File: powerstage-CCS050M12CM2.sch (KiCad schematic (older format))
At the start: 34 parts, among them J13 CONN_01X01, Q2 CCS050M12CM2, U10 74LVC2G04, U11 TXS0108E

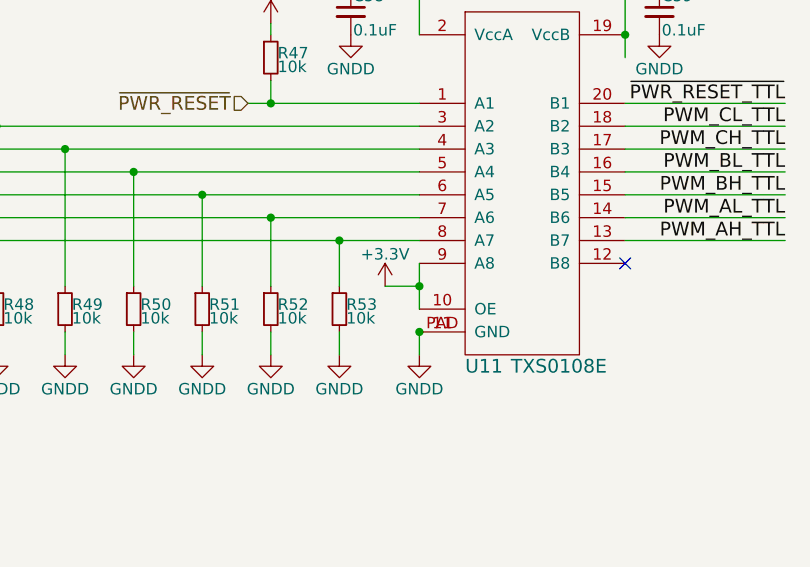
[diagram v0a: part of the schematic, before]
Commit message: stepdown PSU placed
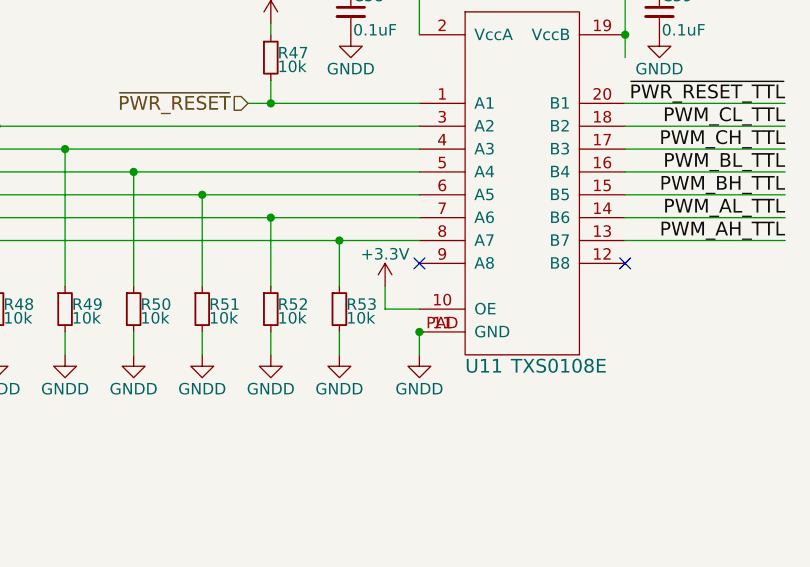
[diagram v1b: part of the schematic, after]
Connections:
- net +3V3: no longer U11.9 (A8)
- no-connect marks 1 -> 2
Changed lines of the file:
@@
 LIBS:TMDSCNCD28069
 LIBS:74LVC8T245
-LIBS:viper0p-etc
 LIBS:sictroller-cache
 EELAYER 25 0
@@
 $EndDescr
 $Comp
-L +5VD #PWR086
+L +5VD #PWR96
 U 1 1 57A1909B
 P 4150 4250
-F 0 "#PWR086" H 4150 4100 50  0001 C CNN
+F 0 "#PWR96" H 4150 4100 50  0001 C CNN
 F 1 "+5VD" H 4150 4390 50  0000 C CNN
 F 2 "" H 4150 4250 50  0000 C CNN
@@
 $EndComp
 $Comp
-L GNDD #PWR087
+L GNDD #PWR92
 U 1 1 57A19106
 P 2950 4550
-F 0 "#PWR087" H 2950 4300 50  0001 C CNN
+F 0 "#PWR92" H 2950 4300 50  0001 C CNN
 F 1 "GNDD" H 2950 4400 50  0000 C CNN
 F 2 "" H 2950 4550 50  0000 C CNN
@@
 $EndComp
 $Comp
-L GNDD #PWR088
+L GNDD #PWR97
 U 1 1 57A1910C
 P 4300 4550
-F 0 "#PWR088" H 4300 4300 50  0001 C CNN
+F 0 "#PWR97" H 4300 4300 50  0001 C CNN
 F 1 "GNDD" H 4300 4400 50  0000 C CNN
 F 2 "" H 4300 4550 50  0000 C CNN
@@
 $EndComp
 $Comp
-L +3.3V #PWR089
+L +3.3V #PWR89
 U 1 1 57A19125
 P 2600 4500
-F 0 "#PWR089" H 2600 4350 50  0001 C CNN
+F 0 "#PWR89" H 2600 4350 50  0001 C CNN
 F 1 "+3.3V" H 2600 4640 50  0000 C CNN
 F 2 "" H 2600 4500 50  0000 C CNN
@@
 $EndComp
 $Comp
-L GNDD #PWR090
+L GNDD #PWR95
 U 1 1 57A19193
 P 3250 5950
-F 0 "#PWR090" H 3250 5700 50  0001 C CNN
+F 0 "#PWR95" H 3250 5700 50  0001 C CNN
 F 1 "GNDD" H 3250 5800 50  0000 C CNN
 F 2 "" H 3250 5950 50  0000 C CNN
@@
 $EndComp
 $Comp
-L +3.3V #PWR091
+L +3.3V #PWR94
 U 1 1 57A19100
 P 3250 4250
-F 0 "#PWR091" H 3250 4100 50  0001 C CNN
+F 0 "#PWR94" H 3250 4100 50  0001 C CNN
 F 1 "+3.3V" H 3250 4390 50  0000 C CNN
 F 2 "" H 3250 4250 50  0000 C CNN
@@
 $EndComp
 $Comp
-L GNDD #PWR092
+L GNDD #PWR86
 U 1 1 57A23C37
 P 2200 2150
-F 0 "#PWR092" H 2200 1900 50  0001 C CNN
+F 0 "#PWR86" H 2200 1900 50  0001 C CNN
 F 1 "GNDD" H 2200 2000 50  0000 C CNN
 F 2 "" H 2200 2150 50  0000 C CNN
@@
 $EndComp
 $Comp
-L +3.3V #PWR093
+L +3.3V #PWR85
 U 1 1 57A23E25
 P 2200 1200
-F 0 "#PWR093" H 2200 1050 50  0001 C CNN
+F 0 "#PWR85" H 2200 1050 50  0001 C CNN
 F 1 "+3.3V" H 2200 1340 50  0000 C CNN
 F 2 "" H 2200 1200 50  0000 C CNN
@@
 $EndComp
 $Comp
-L GNDD #PWR094
+L GNDD #PWR88
 U 1 1 57A244F4
 P 2500 1450
-F 0 "#PWR094" H 2500 1200 50  0001 C CNN
+F 0 "#PWR88" H 2500 1200 50  0001 C CNN
 F 1 "GNDD" H 2500 1300 50  0000 C CNN
 F 2 "" H 2500 1450 50  0000 C CNN
@@
 GDRV_RDY_TTL
 $Comp
-L +5VD #PWR095
+L +5VD #PWR102
 U 1 1 57F46580
 P 5900 4750
-F 0 "#PWR095" H 5900 4600 50  0001 C CNN
+F 0 "#PWR102" H 5900 4600 50  0001 C CNN
 F 1 "+5VD" H 5900 4890 50  0000 C CNN
 F 2 "" H 5900 4750 50  0000 C CNN
@@
 $EndComp
 $Comp
-L GNDD #PWR096
+L GNDD #PWR103
 U 1 1 57F47836
 P 5900 5900
-F 0 "#PWR096" H 5900 5650 50  0001 C CNN
+F 0 "#PWR103" H 5900 5650 50  0001 C CNN
 F 1 "GNDD" H 5900 5750 50  0000 C CNN
 F 2 "" H 5900 5900 50  0000 C CNN
@@
 $EndComp
 $Comp
-L GNDD #PWR097
+L GNDD #PWR101
 U 1 1 57F48803
 P 5900 4000
-F 0 "#PWR097" H 5900 3750 50  0001 C CNN
+F 0 "#PWR101" H 5900 3750 50  0001 C CNN
 F 1 "GNDD" H 5900 3850 50  0000 C CNN
 F 2 "" H 5900 4000 50  0000 C CNN
@@
 $EndComp
 $Comp
-L GNDD #PWR098
+L GNDD #PWR99
 U 1 1 57F497CA
 P 5900 2100
-F 0 "#PWR098" H 5900 1850 50  0001 C CNN
+F 0 "#PWR99" H 5900 1850 50  0001 C CNN
 F 1 "GNDD" H 5900 1950 50  0000 C CNN
 F 2 "" H 5900 2100 50  0000 C CNN
@@
 $EndComp
 $Comp
-L +5VD #PWR099
+L +5VD #PWR100
 U 1 1 57F4B3DF
 P 5900 2850
-F 0 "#PWR099" H 5900 2700 50  0001 C CNN
+F 0 "#PWR100" H 5900 2700 50  0001 C CNN
 F 1 "+5VD" H 5900 2990 50  0000 C CNN
 F 2 "" H 5900 2850 50  0000 C CNN
@@
 $EndComp
 $Comp
-L +5VD #PWR0100
+L +5VD #PWR98
 U 1 1 57F4C376
 P 5900 950
-F 0 "#PWR0100" H 5900 800 50  0001 C CNN
+F 0 "#PWR98" H 5900 800 50  0001 C CNN
 F 1 "+5VD" H 5900 1090 50  0000 C CNN
 F 2 "" H 5900 950 50  0000 C CNN
@@
 $EndComp
 $Comp
-L GNDD #PWR0101
+L GNDD #PWR82
 U 1 1 57F64D21
 P 1400 5950
-F 0 "#PWR0101" H 1400 5700 50  0001 C CNN
+F 0 "#PWR82" H 1400 5700 50  0001 C CNN
 F 1 "GNDD" H 1400 5800 50  0000 C CNN
 F 2 "" H 1400 5950 50  0000 C CNN
@@
 $EndComp
 $Comp
-L GNDD #PWR0102
+L GNDD #PWR83
 U 1 1 57F6CC6B
 P 1700 5950
-F 0 "#PWR0102" H 1700 5700 50  0001 C CNN
+F 0 "#PWR83" H 1700 5700 50  0001 C CNN
 F 1 "GNDD" H 1700 5800 50  0000 C CNN
 F 2 "" H 1700 5950 50  0000 C CNN
@@
 $EndComp
 $Comp
-L GNDD #PWR0103
+L GNDD #PWR84
 U 1 1 57F6CE7E
 P 2000 5950
-F 0 "#PWR0103" H 2000 5700 50  0001 C CNN
+F 0 "#PWR84" H 2000 5700 50  0001 C CNN
 F 1 "GNDD" H 2000 5800 50  0000 C CNN
 F 2 "" H 2000 5950 50  0000 C CNN
@@
 $EndComp
 $Comp
-L GNDD #PWR0104
+L GNDD #PWR87
 U 1 1 57F6CE85
 P 2300 5950
-F 0 "#PWR0104" H 2300 5700 50  0001 C CNN
+F 0 "#PWR87" H 2300 5700 50  0001 C CNN
 F 1 "GNDD" H 2300 5800 50  0000 C CNN
 F 2 "" H 2300 5950 50  0000 C CNN
@@
 $EndComp
 $Comp
-L GNDD #PWR0105
+L GNDD #PWR90
 U 1 1 57F6D098
 P 2600 5950
-F 0 "#PWR0105" H 2600 5700 50  0001 C CNN
+F 0 "#PWR90" H 2600 5700 50  0001 C CNN
 F 1 "GNDD" H 2600 5800 50  0000 C CNN
 F 2 "" H 2600 5950 50  0000 C CNN
@@
 $EndComp
 $Comp
-L GNDD #PWR0106
+L GNDD #PWR91
 U 1 1 57F6D09F
 P 2900 5950
-F 0 "#PWR0106" H 2900 5700 50  0001 C CNN
+F 0 "#PWR91" H 2900 5700 50  0001 C CNN
 F 1 "GNDD" H 2900 5800 50  0000 C CNN
 F 2 "" H 2900 5950 50  0000 C CNN
@@
 $EndComp
 $Comp
-L +3.3V #PWR0107
+L +3.3V #PWR93
 U 1 1 5800C8BD
 P 3100 5650
-F 0 "#PWR0107" H 3100 5500 50  0001 C CNN
+F 0 "#PWR93" H 3100 5500 50  0001 C CNN
 F 1 "+3.3V" H 3100 5790 50  0000 C CNN
 F 2 "" H 3100 5650 50  0000 C CNN
@@
 Wire Wire Line
 	4150 4250 4150 4650
-Wire Wire Line
-	3250 5550 3250 5750
 Wire Wire Line
 	3250 5850 3250 5950
@@
 Wire Wire Line
 	3250 4250 3250 4550
-Wire Wire Line
-	3100 5650 3250 5650
-Connection ~ 3250 5650
 Text Label 9600 6000 0    60   ~ 0
 Y
+Wire Wire Line
+	3100 5650 3100 5750
+Wire Wire Line
+	3100 5750 3250 5750
+NoConn ~ 3250 5550
 $EndSCHEMATC

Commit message: Add more ceralinks on rear
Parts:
- added C79, C80, C81, C82, C83, C84, C85, C86, C87, C88, C89, C90: 1uF, sictroller:Ceralink-L, symbol C_Small
- renumbered C57 to C58, C58 to C59, C59 to C60, C60 to C61, C61 to C62, C62 to C63, C63 to C64, C64 to C65, C65 to C66, C66 to C67, C67 to C68, C68 to C69, C69 to C70, C70 to C71, C71 to C72, C72 to C73, C73 to C74, C74 to C75, C75 to C76, C76 to C77, C77 to C78, R47 to R49, R48 to R50, R49 to R51, R50 to R52, R51 to R53, R52 to R54, R53 to R55, R54 to R56, R55 to R57
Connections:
- net BUS+: now also C79.1, C80.1, C81.1, C82.1, C83.1, C84.1, C85.1, C86.1, C87.1, C88.1, C89.1, C90.1
- net BUS-: now also C79.2, C80.2, C81.2, C82.2, C83.2, C84.2, C85.2, C86.2, C87.2, C88.2, C89.2, C90.2
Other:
- note added: "DC-link bypass caps, top side"
- note added: "bottom side"

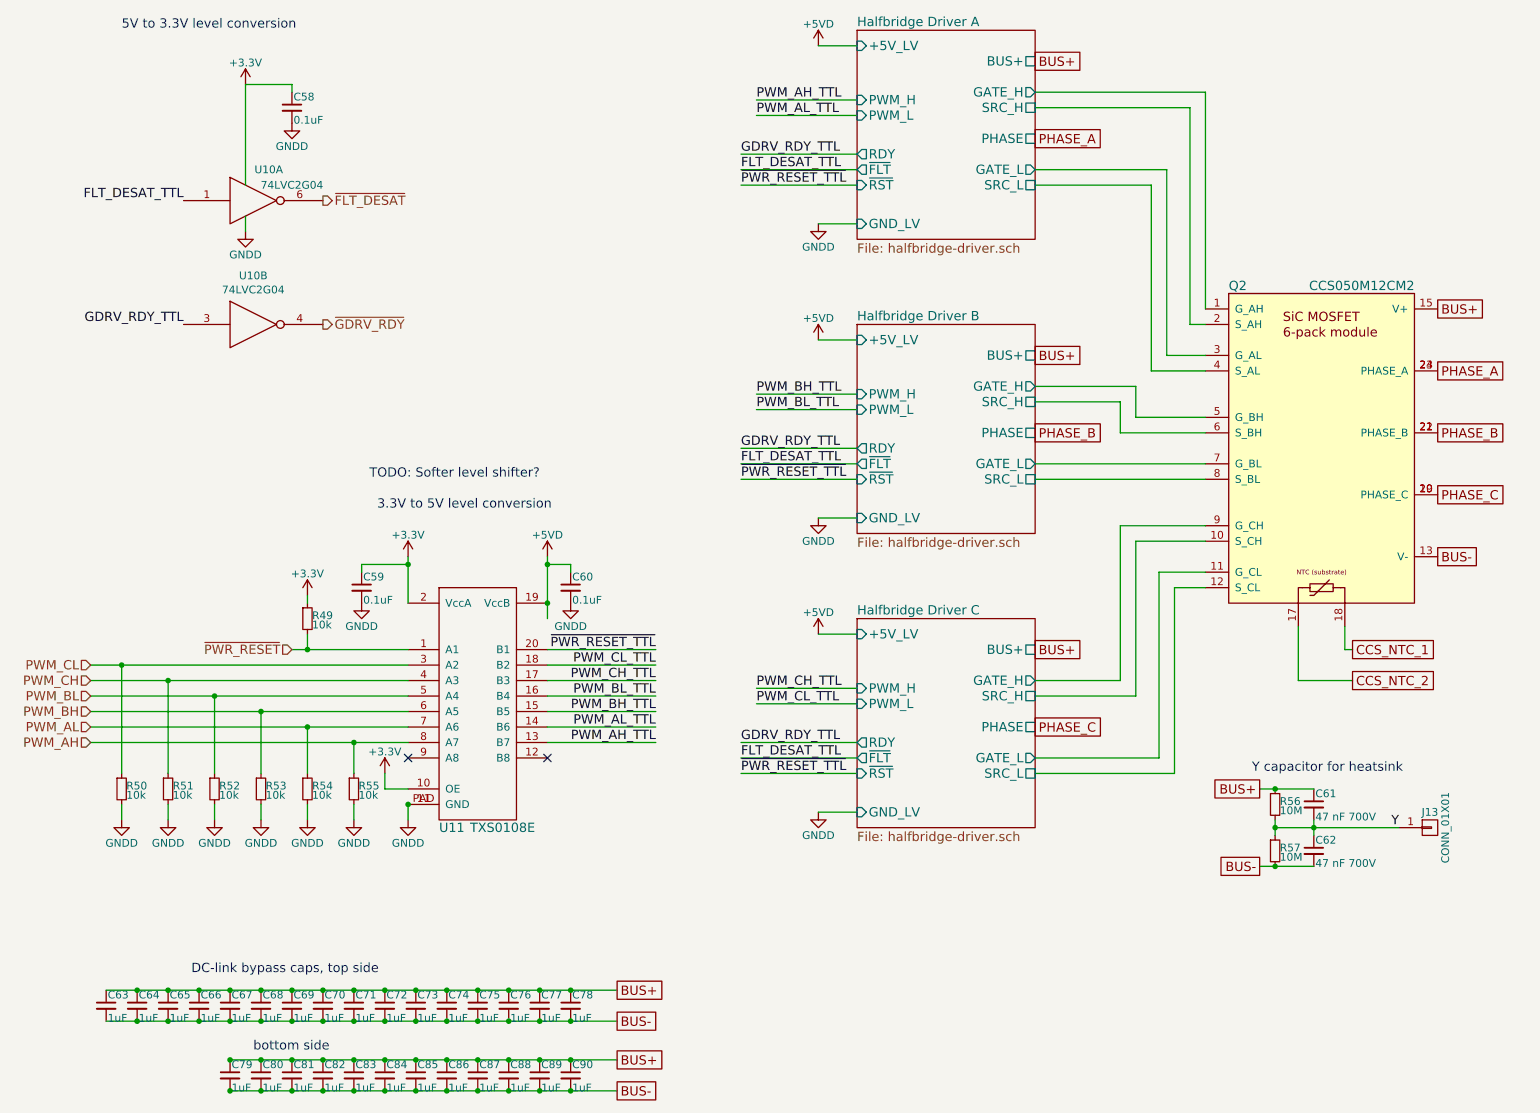
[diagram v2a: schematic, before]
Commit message: Add 1568 vias in DC link cap pads
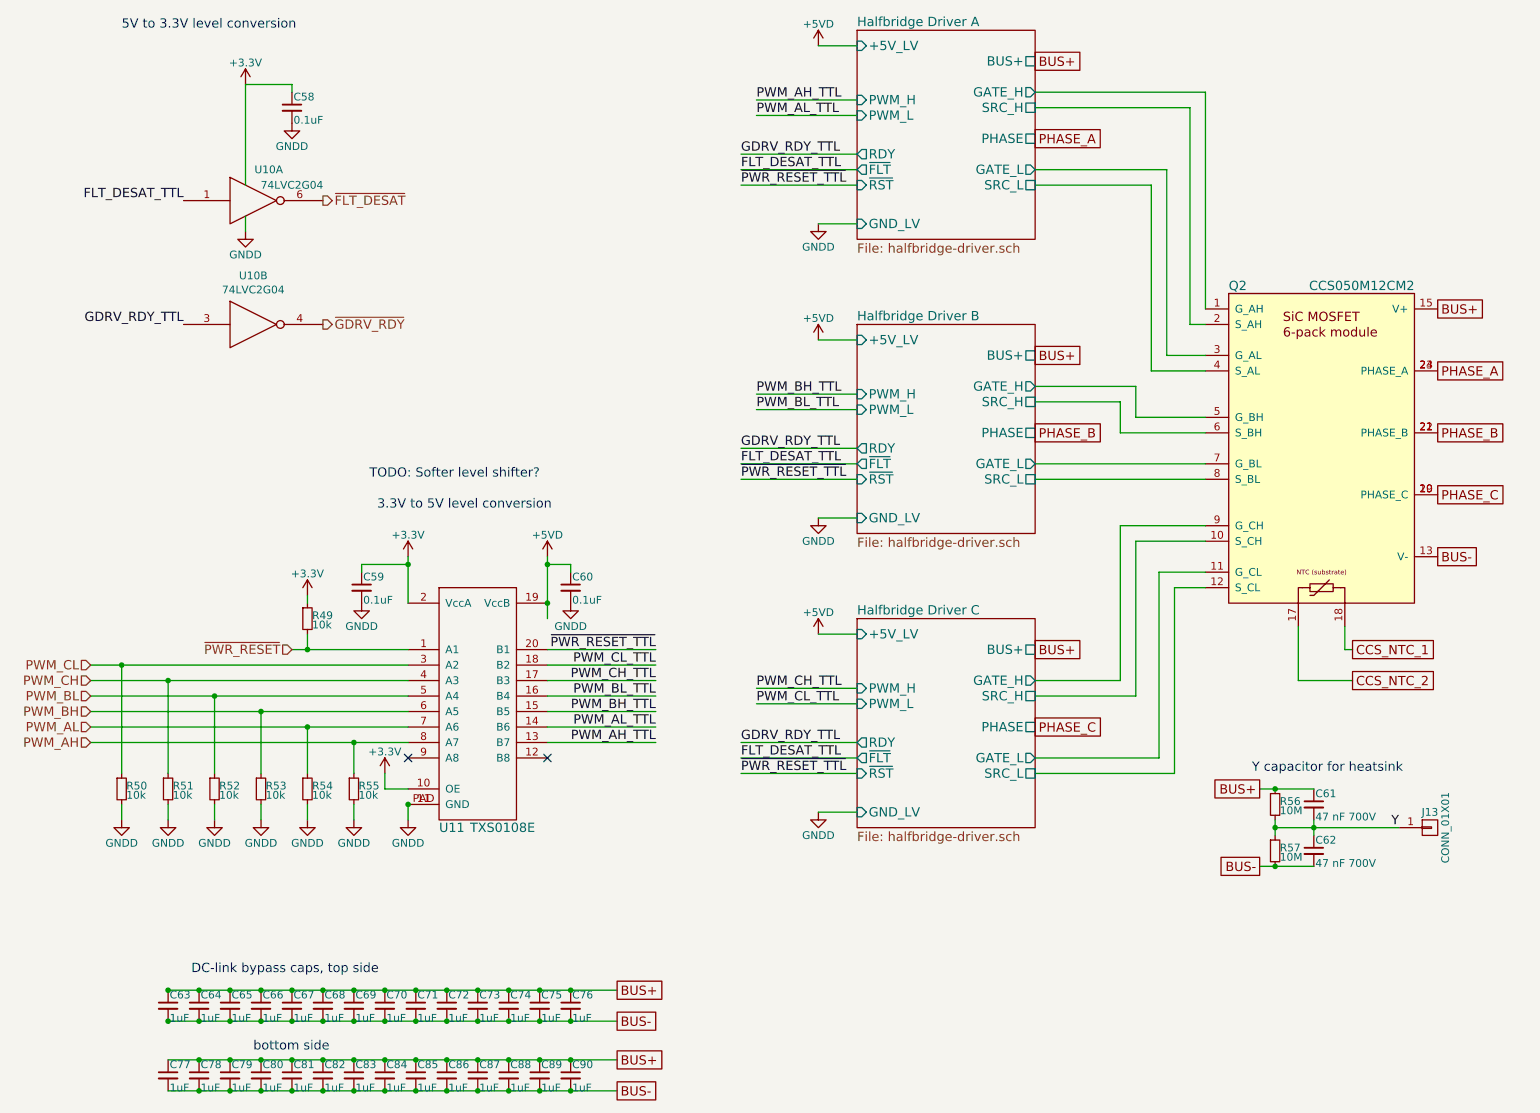
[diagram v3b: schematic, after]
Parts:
- C63: renamed from C65; footprint sictroller:Ceralink-L -> sictroller:Ceralink-L-viastitch
- renumbered C66 to C64, C67 to C65, C68 to C66, C69 to C67, C70 to C68, C71 to C69, C72 to C70, C73 to C71, C74 to C72, C75 to C73, C76 to C74, C77 to C75, C78 to C76, C63 to C77, C64 to C78
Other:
- moved on the sheet: C77, C78

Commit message: Improved footprint for B6A-PCB
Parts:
- C64, C65, C66, C67, C68, C69, C70, C71, C72, C73, C74, C75, C76: footprint sictroller:Ceralink-L -> sictroller:Ceralink-L-viastitch
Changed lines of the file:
@@
 F 0 "C64" H 1910 7220 50  0000 L CNN
 F 1 "1uF" H 1910 7070 50  0000 L CNN
-F 2 "sictroller:Ceralink-L" H 1900 7150 50  0001 C CNN
+F 2 "sictroller:Ceralink-L-viastitch" H 1900 7150 50  0001 C CNN
 F 3 "" H 1900 7150 50  0000 C CNN
 	1    1900 7150
@@
 F 0 "C65" H 2110 7220 50  0000 L CNN
 F 1 "1uF" H 2110 7070 50  0000 L CNN
-F 2 "sictroller:Ceralink-L" H 2100 7150 50  0001 C CNN
+F 2 "sictroller:Ceralink-L-viastitch" H 2100 7150 50  0001 C CNN
 F 3 "" H 2100 7150 50  0000 C CNN
 	1    2100 7150
@@
 F 0 "C66" H 2310 7220 50  0000 L CNN
 F 1 "1uF" H 2310 7070 50  0000 L CNN
-F 2 "sictroller:Ceralink-L" H 2300 7150 50  0001 C CNN
+F 2 "sictroller:Ceralink-L-viastitch" H 2300 7150 50  0001 C CNN
 F 3 "" H 2300 7150 50  0000 C CNN
 	1    2300 7150
@@
 F 0 "C67" H 2510 7220 50  0000 L CNN
 F 1 "1uF" H 2510 7070 50  0000 L CNN
-F 2 "sictroller:Ceralink-L" H 2500 7150 50  0001 C CNN
+F 2 "sictroller:Ceralink-L-viastitch" H 2500 7150 50  0001 C CNN
 F 3 "" H 2500 7150 50  0000 C CNN
 	1    2500 7150
@@
 F 0 "C68" H 2710 7220 50  0000 L CNN
 F 1 "1uF" H 2710 7070 50  0000 L CNN
-F 2 "sictroller:Ceralink-L" H 2700 7150 50  0001 C CNN
+F 2 "sictroller:Ceralink-L-viastitch" H 2700 7150 50  0001 C CNN
 F 3 "" H 2700 7150 50  0000 C CNN
 	1    2700 7150
@@
 F 0 "C69" H 2910 7220 50  0000 L CNN
 F 1 "1uF" H 2910 7070 50  0000 L CNN
-F 2 "sictroller:Ceralink-L" H 2900 7150 50  0001 C CNN
+F 2 "sictroller:Ceralink-L-viastitch" H 2900 7150 50  0001 C CNN
 F 3 "" H 2900 7150 50  0000 C CNN
 	1    2900 7150
@@
 F 0 "C70" H 3110 7220 50  0000 L CNN
 F 1 "1uF" H 3110 7070 50  0000 L CNN
-F 2 "sictroller:Ceralink-L" H 3100 7150 50  0001 C CNN
+F 2 "sictroller:Ceralink-L-viastitch" H 3100 7150 50  0001 C CNN
 F 3 "" H 3100 7150 50  0000 C CNN
 	1    3100 7150
@@
 F 0 "C71" H 3310 7220 50  0000 L CNN
 F 1 "1uF" H 3310 7070 50  0000 L CNN
-F 2 "sictroller:Ceralink-L" H 3300 7150 50  0001 C CNN
+F 2 "sictroller:Ceralink-L-viastitch" H 3300 7150 50  0001 C CNN
 F 3 "" H 3300 7150 50  0000 C CNN
 	1    3300 7150
@@
 F 0 "C72" H 3510 7220 50  0000 L CNN
 F 1 "1uF" H 3510 7070 50  0000 L CNN
-F 2 "sictroller:Ceralink-L" H 3500 7150 50  0001 C CNN
+F 2 "sictroller:Ceralink-L-viastitch" H 3500 7150 50  0001 C CNN
 F 3 "" H 3500 7150 50  0000 C CNN
 	1    3500 7150
@@
 F 0 "C73" H 3710 7220 50  0000 L CNN
 F 1 "1uF" H 3710 7070 50  0000 L CNN
-F 2 "sictroller:Ceralink-L" H 3700 7150 50  0001 C CNN
+F 2 "sictroller:Ceralink-L-viastitch" H 3700 7150 50  0001 C CNN
 F 3 "" H 3700 7150 50  0000 C CNN
 	1    3700 7150
@@
 F 0 "C74" H 3910 7220 50  0000 L CNN
 F 1 "1uF" H 3910 7070 50  0000 L CNN
-F 2 "sictroller:Ceralink-L" H 3900 7150 50  0001 C CNN
+F 2 "sictroller:Ceralink-L-viastitch" H 3900 7150 50  0001 C CNN
 F 3 "" H 3900 7150 50  0000 C CNN
 	1    3900 7150
@@
 F 0 "C75" H 4110 7220 50  0000 L CNN
 F 1 "1uF" H 4110 7070 50  0000 L CNN
-F 2 "sictroller:Ceralink-L" H 4100 7150 50  0001 C CNN
+F 2 "sictroller:Ceralink-L-viastitch" H 4100 7150 50  0001 C CNN
 F 3 "" H 4100 7150 50  0000 C CNN
 	1    4100 7150
@@
 F 0 "C76" H 4310 7220 50  0000 L CNN
 F 1 "1uF" H 4310 7070 50  0000 L CNN
-F 2 "sictroller:Ceralink-L" H 4300 7150 50  0001 C CNN
+F 2 "sictroller:Ceralink-L-viastitch" H 4300 7150 50  0001 C CNN
 F 3 "" H 4300 7150 50  0000 C CNN
 	1    4300 7150
